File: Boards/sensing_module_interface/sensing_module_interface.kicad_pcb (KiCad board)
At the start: 2 copper layers, 109.3 x 58.3 mm, 19 parts, among them U101 TPS560430YF

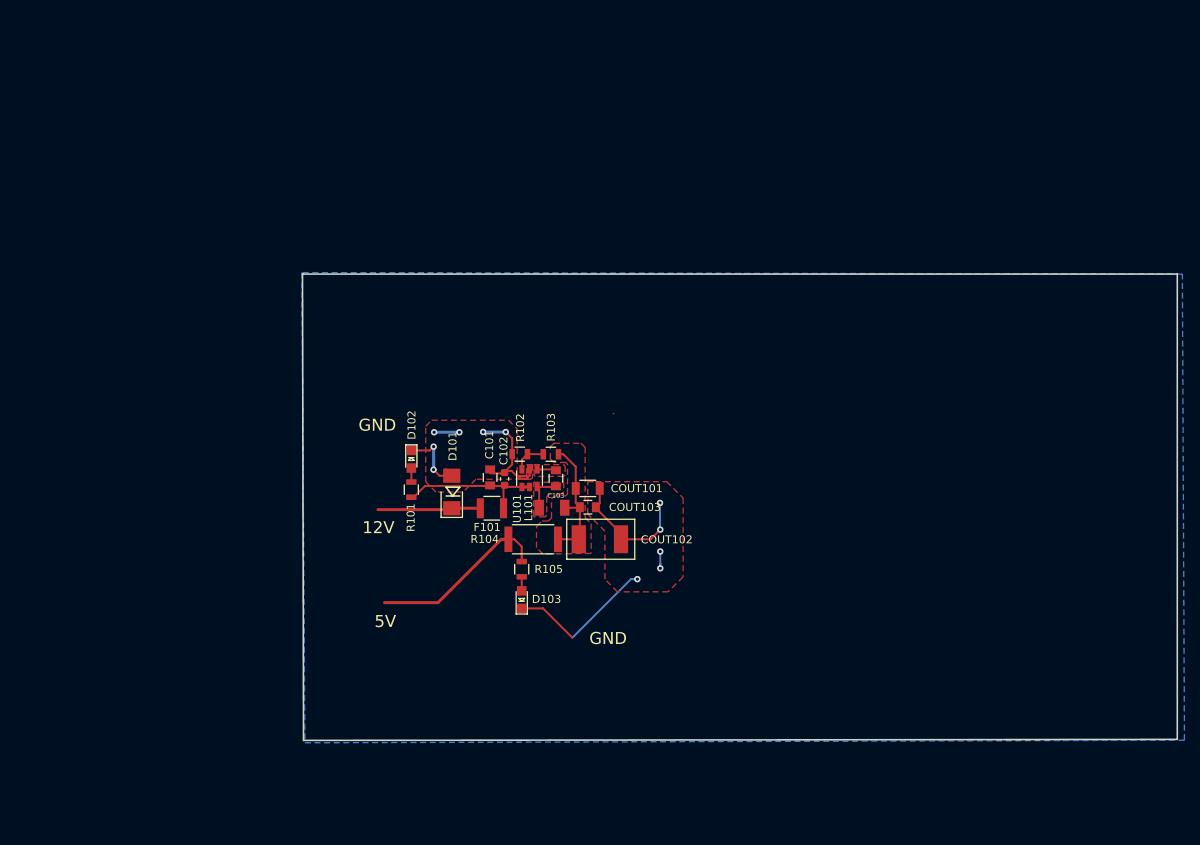
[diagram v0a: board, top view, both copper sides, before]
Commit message: updated schematic with 4 more gauges, started layout
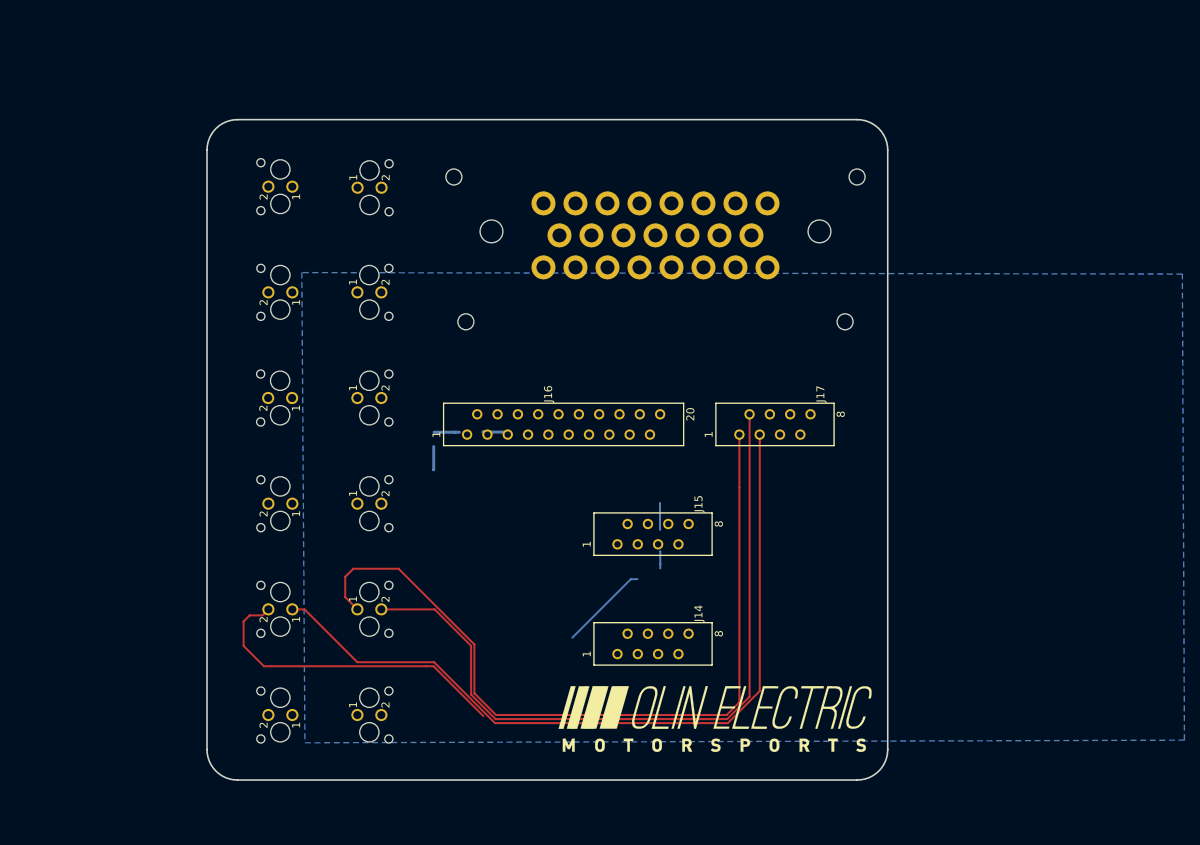
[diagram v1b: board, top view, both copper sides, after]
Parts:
- removed C101, C103: C_0.1uF, footprints:C_0805_OEM
- removed C102: C_2.2uF, footprints:C_0603_1608Metric
- removed COUT101: C_22uF, footprints:C_1206_OEM
- removed COUT102: C_33uF, footprints:Fuse_1812
- removed COUT103: C_47uF, footprints:C_0805_OEM
- removed D101: D_Zener_18V, footprints:DO-214AA
- removed D102, D103: LED_0805, footprints:LED_0805_OEM
- removed F101: F_500mA_16V, footprints:Fuse_1210
- removed the G*** at (179.6, 107.2)
- removed L101: L_100uH, footprints:L_100uH
- removed R101, R105: R_200, footprints:R_0805_OEM
- removed R102: R_25K, footprints:R_0805_OEM
- removed R103: R_100K, footprints:R_0805_OEM
- removed R104: R_0_2512, footprints:R_2512_OEM
- removed U101: TPS560430YF, footprints:SOT-23-6_OEM
- added J1: Ampseal_23_VT, footprints:Ampseal_23, B.Cu at (121.9, 71.1)
- added J10: MicroFit_V_2, footprints:MicroFit_V_2, B.Cu at (105.2, 118.4)
- added J11: MicroFit_V_2, footprints:MicroFit_V_2, B.Cu at (97.0, 118.4)
- added J12: MicroFit_V_2, footprints:MicroFit_V_2, B.Cu at (105.2, 131.6)
- added J13: MicroFit_V_2, footprints:MicroFit_V_2, B.Cu at (97.0, 131.6)
- added J14: MM_M_VT_08, footprints:micromatch_female_ra_8, F.Cu at (142.7, 124.0)
- added J15: MM_M_VT_08, footprints:micromatch_female_ra_8, F.Cu at (142.7, 110.2)
- added J16: MM_M_VT_20, footprints:micromatch_female_ra_20, F.Cu at (124.0, 96.5)
- added J17: MM_M_VT_08, footprints:micromatch_female_ra_8, F.Cu at (158.0, 96.5)
- added J2: MicroFit_V_2, footprints:MicroFit_V_2, B.Cu at (105.2, 65.7)
- added J3: MicroFit_V_2, footprints:MicroFit_V_2, B.Cu at (97.0, 65.5)
- added J4: MicroFit_V_2, footprints:MicroFit_V_2, B.Cu at (105.2, 78.7)
- added J5: MicroFit_V_2, footprints:MicroFit_V_2, B.Cu at (97.0, 78.7)
- added J6: MicroFit_V_2, footprints:MicroFit_V_2, B.Cu at (105.2, 91.9)
- added J7: MicroFit_V_2, footprints:MicroFit_V_2, B.Cu at (97.0, 91.9)
- added J8: MicroFit_V_2, footprints:MicroFit_V_2, B.Cu at (105.2, 105.2)
- added J9: MicroFit_V_2, footprints:MicroFit_V_2, B.Cu at (97.0, 105.2)
- G***: moved to F.Cu
- moved G*** 55.1 mm to (149.9, 132.1), turned to 0 degrees
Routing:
- net /STRAIN_GAUGE_9_+: track 0.00 -> 99.7 mm
- net /STRAIN_GAUGE_10_+: track 0.00 -> 98.0 mm
- net /STRAIN_GAUGE_9_-: track 0.00 -> 91.7 mm
- net /STRAIN_GAUGE_10_-: track 0.00 -> 40.4 mm
- net GND: track 65.5 -> 25.5 mm, vias 11 -> 0
- net VCC: track 22.7 -> 0.00 mm
- net Net-(C101-Pad1): track 18.1 -> 0.00 mm
- net Net-(COUT101-Pad1): track 17.3 -> 0.00 mm
- net /12V: track 12.9 -> 0.00 mm
- net Net-(C103-Pad2): track 5.44 -> 0.00 mm
- net Net-(R102-Pad1): track 4.18 -> 0.00 mm
- net Net-(C103-Pad1): track 2.39 -> 0.00 mm
- net Net-(D103-Pad2): track 1.75 -> 0.00 mm
- net Net-(D102-Pad2): track 1.75 -> 0.00 mm
- removed copper zone on F.Cu, net GND
- removed copper zone on F.Cu, net Net-(C103-Pad1)
- removed copper zone on F.Cu, net Net-(C103-Pad2)
- removed copper zone on F.Cu, net Net-(COUT101-Pad1)
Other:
- board size 109.3 x 58.3 mm -> 85.1 x 82.6 mm
- board text removed: "12V"
- board text removed: "5V"
- board text removed: "GND"

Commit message: layout done, need to review against checklist
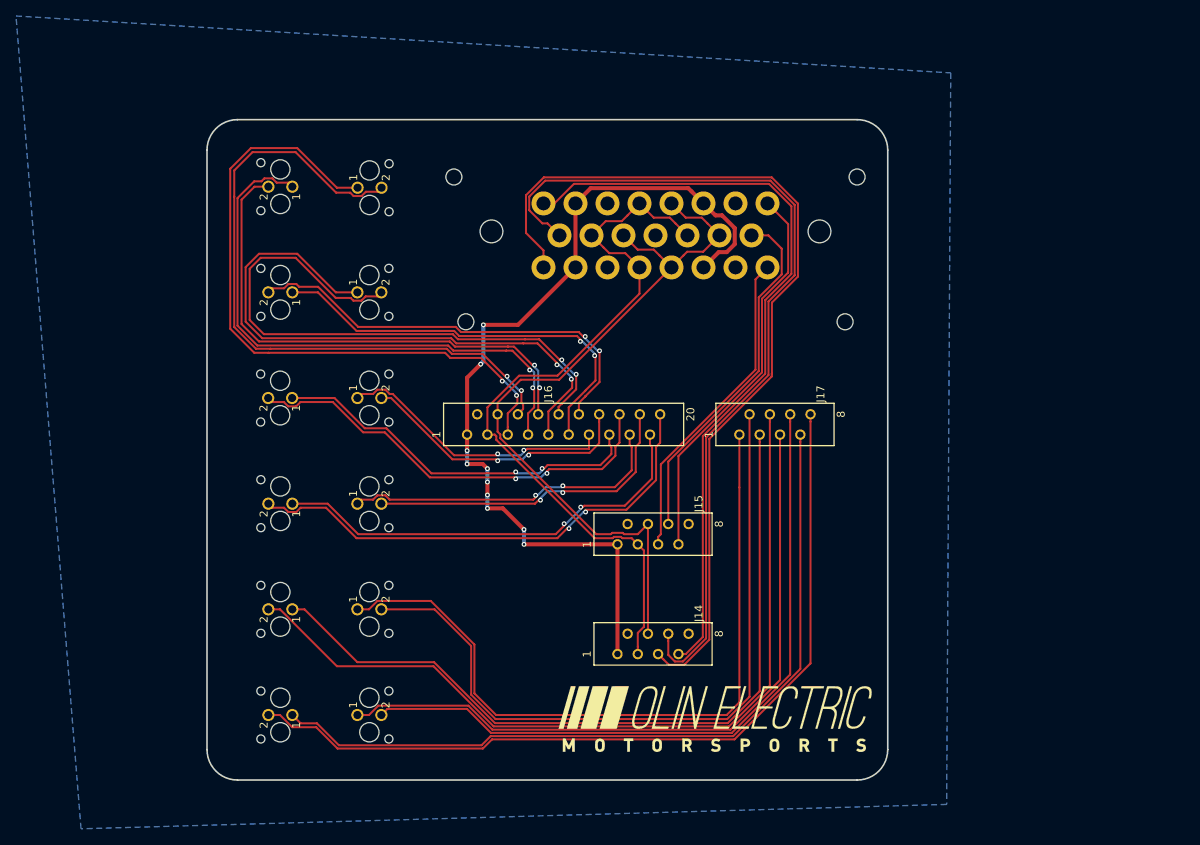
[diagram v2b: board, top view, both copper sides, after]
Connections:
- net /CAN_HIGH renamed /CAN_P
- net /CAN_LOW renamed /CAN_N
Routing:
- net /HALL_EFFECT_+: track 0.00 -> 113.6 mm
- net /12V: track 0.00 -> 111.3 mm, vias 0 -> 10
- net /HALL_EFFECT_SENSE: track 0.00 -> 109.7 mm
- net /STRAIN_GAUGE_12_-: track 0.00 -> 105.0 mm
- net /STRAIN_GAUGE_12_+: track 0.00 -> 98.3 mm
- net /HALL_EFFECT_-: track 0.00 -> 95.5 mm
- net /CAN_N: track 0.00 -> 94.1 mm
- net /CAN_P: track 0.00 -> 93.8 mm
- net /STRAIN_GAUGE_11_-: track 0.00 -> 88.2 mm
- net /STRAIN_GAUGE_11_+: track 0.00 -> 87.8 mm
- net /STRAIN_GAUGE_1_-: track 0.00 -> 84.3 mm, vias 0 -> 2
- net /STRAIN_GAUGE_1_+: track 0.00 -> 84.0 mm, vias 0 -> 2
- net /STRAIN_GAUGE_3_-: track 0.00 -> 75.8 mm, vias 0 -> 2
- net /STRAIN_GAUGE_3_+: track 0.00 -> 75.7 mm, vias 0 -> 2
- net /STRAIN_GAUGE_2_+: track 0.00 -> 72.1 mm, vias 0 -> 2
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- added copper zone on B.Cu, net /GND
- removed copper zone on B.Cu, net GND
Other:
- net class Default: trace_width 0.1524 -> 0.254

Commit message: finished schematic checklist
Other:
- board text added: "CHECK BOARD ORIENTATION BEFORE PLUGGING IN AND POWERING ON"
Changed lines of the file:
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@@
   (general
     (thickness 1.6)
-    (drawings 26)
+    (drawings 28)
     (tracks 575)
     (zones 0)
@@
   (page A4)
   (layers
-    (0 F.Cu signal)
-    (31 B.Cu signal)
+    (0 F.Cu signal hide)
+    (31 B.Cu signal hide)
     (32 B.Adhes user)
     (33 F.Adhes user)
@@
   (module footprints:micromatch_female_ra_8 (layer F.Cu)
     (at 142.748 110.236 90)
-    (fp_text reference J15 (at 5.08 5.08 90) (layer F.SilkS)
+    (fp_text reference J15 (at 0 8.128 90) (layer F.SilkS)
       (effects (font (size 1 1) (thickness 0.15)))
     )
@@
   (module footprints:micromatch_female_ra_8 (layer F.Cu)
     (at 142.748 123.952 90)
-    (fp_text reference J14 (at 5.08 5.08 90) (layer F.SilkS)
+    (fp_text reference J14 (at 0 8.128 90) (layer F.SilkS)
       (effects (font (size 1 1) (thickness 0.15)))
     )
@@
   (module footprints:micromatch_female_ra_20 (layer F.Cu)
     (at 123.952 96.52 90)
-    (fp_text reference J16 (at 5.08 5.08 90) (layer F.SilkS)
+    (fp_text reference J16 (at 5.588 -6.096 90) (layer F.SilkS)
       (effects (font (size 1 1) (thickness 0.15)))
     )
@@
     )
   )
+  (gr_text "CHECK BOARD ORIENTATION BEFORE\nPLUGGING IN AND POWERING ON" (at 140.716 116.84) (layer F.SilkS)
+    (effects (font (size 1.5 1.5) (thickness 0.3)))
+  )
+  (gr_text "CHECK BOARD ORIENTATION BEFORE\nPLUGGING IN AND POWERING ON" (at 140.716 103.632) (layer F.SilkS)
+    (effects (font (size 1.5 1.5) (thickness 0.3)))
+  )
   (dimension 8.128 (width 0.15) (layer Dwgs.User)

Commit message: V0, finished checklist
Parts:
- moved G*** 2.09 mm to (150.4, 134.1)
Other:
- outline, holes or cut-outs redrawn
- board text added: "1"
- board text added: "20"
- board text added: "8"
- board text added: "Lucky Jordan | 11/15/19 | MKV Sensing Module Interface V0"
- board text removed: "CHECK BOARD ORIENTATION BEFORE PLUGGING IN AND POWERING ON"

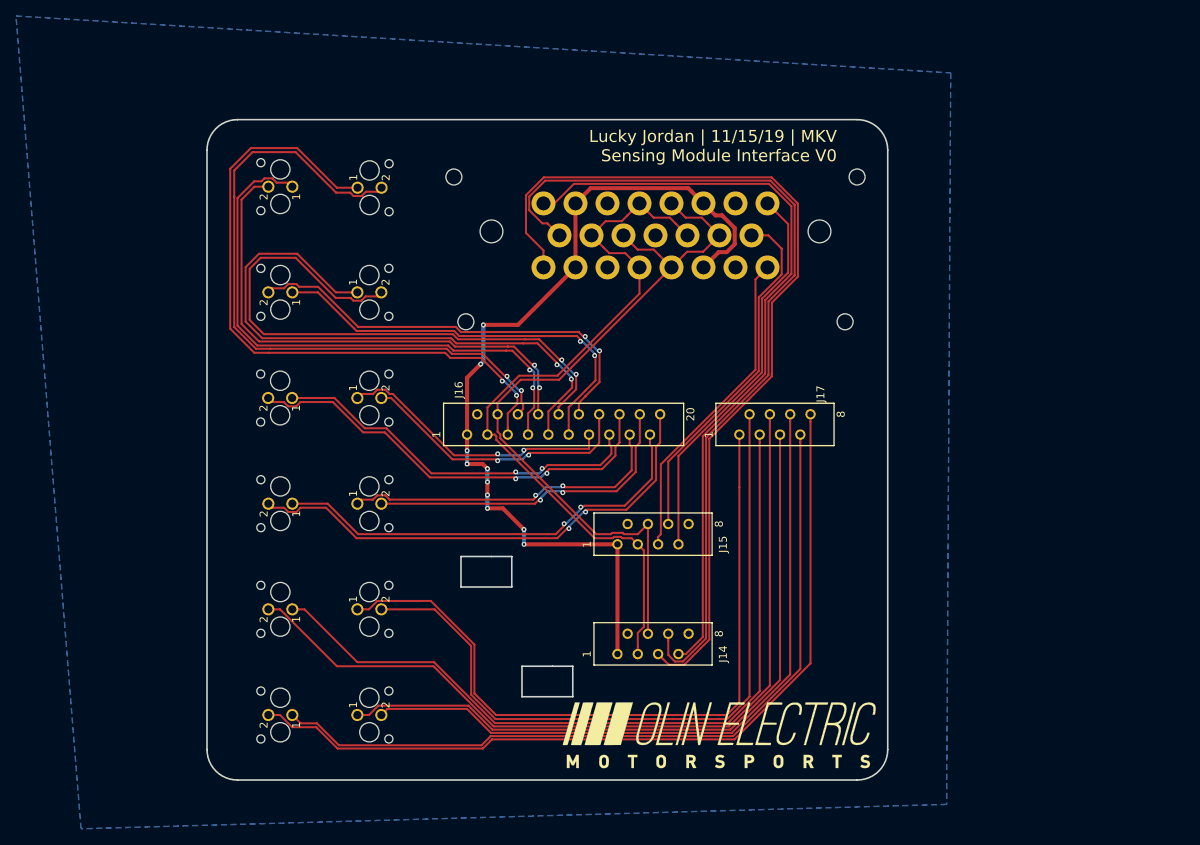
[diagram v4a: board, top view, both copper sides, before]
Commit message: fixed microfits on sensing mod int to give more clearance for latch
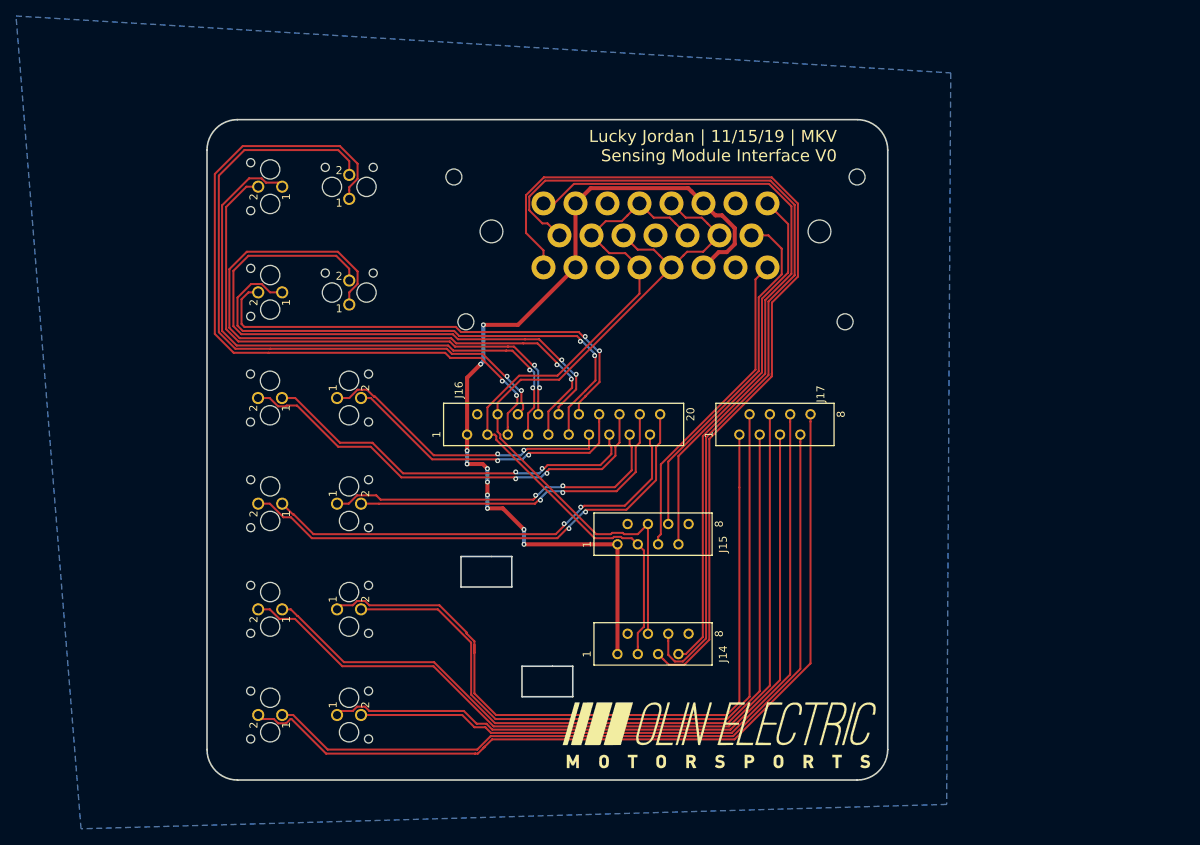
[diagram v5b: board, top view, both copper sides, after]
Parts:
- moved J10 2.54 mm to (102.6, 118.4)
- moved J12 2.54 mm to (102.6, 131.6)
- moved J6 2.54 mm to (102.6, 91.9)
- moved J8 2.54 mm to (102.6, 105.2)
- moved J4 1.83 mm to (104.1, 80.3), turned to 180 degrees
- moved J2 1.74 mm to (104.1, 67.1), turned to 180 degrees
- moved J11 1.27 mm to (95.8, 118.4)
- moved J13 1.27 mm to (95.8, 131.6)
- moved J3 1.27 mm to (95.8, 65.5)
- moved J5 1.27 mm to (95.8, 78.7)
- moved J9 1.27 mm to (95.8, 105.2)
- moved J7 1.27 mm to (95.7, 91.9)
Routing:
- net /STRAIN_GAUGE_4_+: track 52.7 -> 68.0 mm
- net /STRAIN_GAUGE_3_+: track 75.7 -> 83.8 mm
- net /STRAIN_GAUGE_1_+: track 84.0 -> 91.7 mm
- net /STRAIN_GAUGE_4_-: track 54.4 -> 60.8 mm
- net /STRAIN_GAUGE_9_+: track 91.8 -> 95.7 mm
- net /STRAIN_GAUGE_9_-: track 91.7 -> 94.5 mm
- net /STRAIN_GAUGE_12_-: track 105.0 -> 107.6 mm
- net /STRAIN_GAUGE_7_+: track 41.3 -> 43.9 mm
- net /STRAIN_GAUGE_5_-: track 35.2 -> 37.7 mm
- net /STRAIN_GAUGE_5_+: track 35.2 -> 37.7 mm
- net /STRAIN_GAUGE_7_-: track 41.2 -> 43.7 mm
- net /STRAIN_GAUGE_11_+: track 87.8 -> 90.2 mm
- net /STRAIN_GAUGE_2_-: track 64.8 -> 67.2 mm
- net /STRAIN_GAUGE_2_+: track 72.1 -> 74.6 mm
- net /STRAIN_GAUGE_11_-: track 88.2 -> 90.1 mm
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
